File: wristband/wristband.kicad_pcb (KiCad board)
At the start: 2 copper layers, 0 parts

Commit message: Migrate wristband to NINA-B400, wire all sheets, close six design gaps
Replaces the wristband's u-blox NINA-B111 (nRF52832) with a NINA-B400-00B
(Nordic nRF52833, Bluetooth 5.1), then follows through on everything that
change and a full schematic review surfaced.

NINA-B400 migration
- New 55-pin + EGP + EAGP symbol, transcribed from the real NINA-B40 data
  sheet UBX-19049405 R09 Table 6 and cross-checked against Figure 3 for rank
  ordering. Pin numbering validated programmatically (1-55, each exactly once).
- NINA-B4 is pin/mechanically compatible with NINA-B3, NOT NINA-B1, so the
  42-pad NINA111-42 land pattern does not carry over. No official footprint
  exists anywhere -- u-blox's own Eagle library ships only NINA111-42/112-42,
  and neither KiCad's bundled nor upstream RF_Module library has a B3/B4 part.
  NINA-B400-55_PLACEHOLDER is therefore flagged: outline, pad count and rank
  arrangement are confirmed; individual pad X/Y are derived estimates.
  MUST be replaced before fabrication.
- B400 chosen over B401/B406 for its on-module U.FL connector, which let the
  PCB-side U.FL (J2) and the untuned L/C match network (L1/C13) be deleted --
  retiring the project's only open RF-tuning risk.
- No power-design impact: abs-max VCC is 3.9 V on both modules, so the MCP1700
  LDO rationale stands. Budget 12 mA -> 15.5 mA typ; ~70.5 mA with DWM3000
  against 250 mA, ~3.5x headroom (corrects a stale "3.7x" in the docs).
- SWD pin numbers are unchanged (SWDCLK=11, SWDIO=15, RESET_N=19, SWO=8).

Antenna re-verified, part number corrected
- The specified antenna is still pre-approved for NINA-B4 (certification app
  note UBX-20037320 R05 s3.2) but ProAnt was acquired by Abracon and u-blox
  now lists it as PRO-IS-237. Same specs throughout. Order under the Abracon PN.

Six gaps closed
- Y1 + C14/C15: 32.768 kHz LFXO (Epson FC-135, Q13FC13500004). Required for
  lowest sleep current per SIM UBX-19052230 R13 s1.9; XL1/XL2 were floating,
  which Table 6 does not permit eve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
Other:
- board outline added: 45 x 35 mm
- copper layers 2 -> 4
- board text added: "Wristband v0 -- 45 x 35 mm, 4-layer. Stackup intent: F.Cu signal / In1.Cu GND plane / In2.Cu power / B.Cu signal. Solid In1.Cu ground reference is required under the DWM3000 UWB and NINA-B400 BLE sections. Outline and size are a STARTING POINT -- confirm against enclosure and strap before layout."
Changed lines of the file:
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@@
 	(layers
 		(0 "F.Cu" signal)
+		(1 "In1.Cu" signal)
+		(2 "In2.Cu" signal)
 		(31 "B.Cu" signal)
 		(32 "B.Adhes" user "B.Adhesive")
@@
 	)
 	(net 0 "")
+	(gr_line
+		(start 100 60)
+		(end 145 60)
+		(stroke
+			(width 0.1)
+			(type default)
+		)
+		(layer "Edge.Cuts")
+	)
+	(gr_line
+		(start 145 60)
+		(end 145 95)
+		(stroke
+			(width 0.1)
+			(type default)
+		)
+		(layer "Edge.Cuts")
+	)
+	(gr_line
+		(start 145 95)
+		(end 100 95)
+		(stroke
+			(width 0.1)
+			(type default)
+		)
+		(layer "Edge.Cuts")
+	)
+	(gr_line
+		(start 100 95)
+		(end 100 60)
+		(stroke
+			(width 0.1)
+			(type default)
+		)
+		(layer "Edge.Cuts")
+	)
+	(gr_text "Wristband v0 -- 45 x 35 mm, 4-layer.\nStackup intent: F.Cu signal / In1.Cu GND plane / In2.Cu power / B.Cu signal.\nSolid In1.Cu ground reference is required under the DWM3000 UWB and NINA-B400 BLE sections.\nOutline and size are a STARTING POINT -- confirm against enclosure and strap before layout."
+		(at 100 101 0)
+		(layer "Cmts.User")
+		(effects
+			(font
+				(size 1.2 1.2)
+				(thickness 0.2)
+			)
+			(justify left)
+		)
+	)
 )

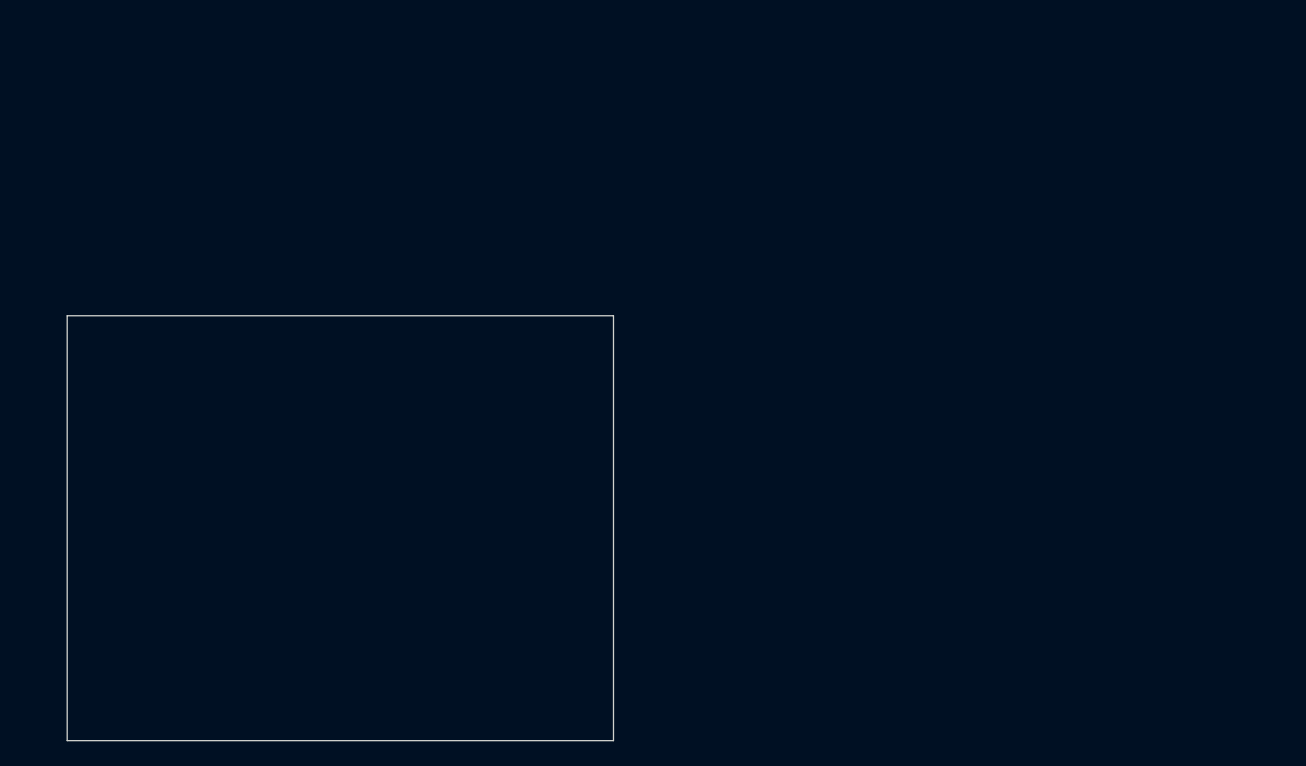
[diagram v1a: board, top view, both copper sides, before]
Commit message: Convert global labels to power symbols; import footprints to PCB
Continues the ground cleanup from 0263e7f across the rest of the wristband
sheets: global labels replaced with explicit power symbols and wired
junctions, so connections are drawn rather than implied by name.

                     wires      labels      junctions   symbols
  power_bms          61 -> 83   61 -> 51    0 -> 3      25 -> 36
  programming_debug   7 ->  8    7 ->  4    0 -> 1       1 ->  3
  radio_mcu          71 -> 79   64 -> 42    7 -> 17     18 -> 32
  regulation          7 ->  7    7 ->  4    0 -> 0       3 ->  6

The added symbols are all power ports, so the BOM is untouched: still 47
components, 76 nets, 42 no-connects, 35 analyzer findings with 1 error --
identical before and after. The one error is the known DW01A false
positive (U1.6 GND sits on CELL_N by design, per the reference circuit).

Also ran Update PCB from Schematic on the wristband: 0 -> 46 footprints.
Nothing routed yet, no zones, board outline unchanged.

Co-Authored-By: Claude Opus 5 (1M context) <noreply@anthropic.com>
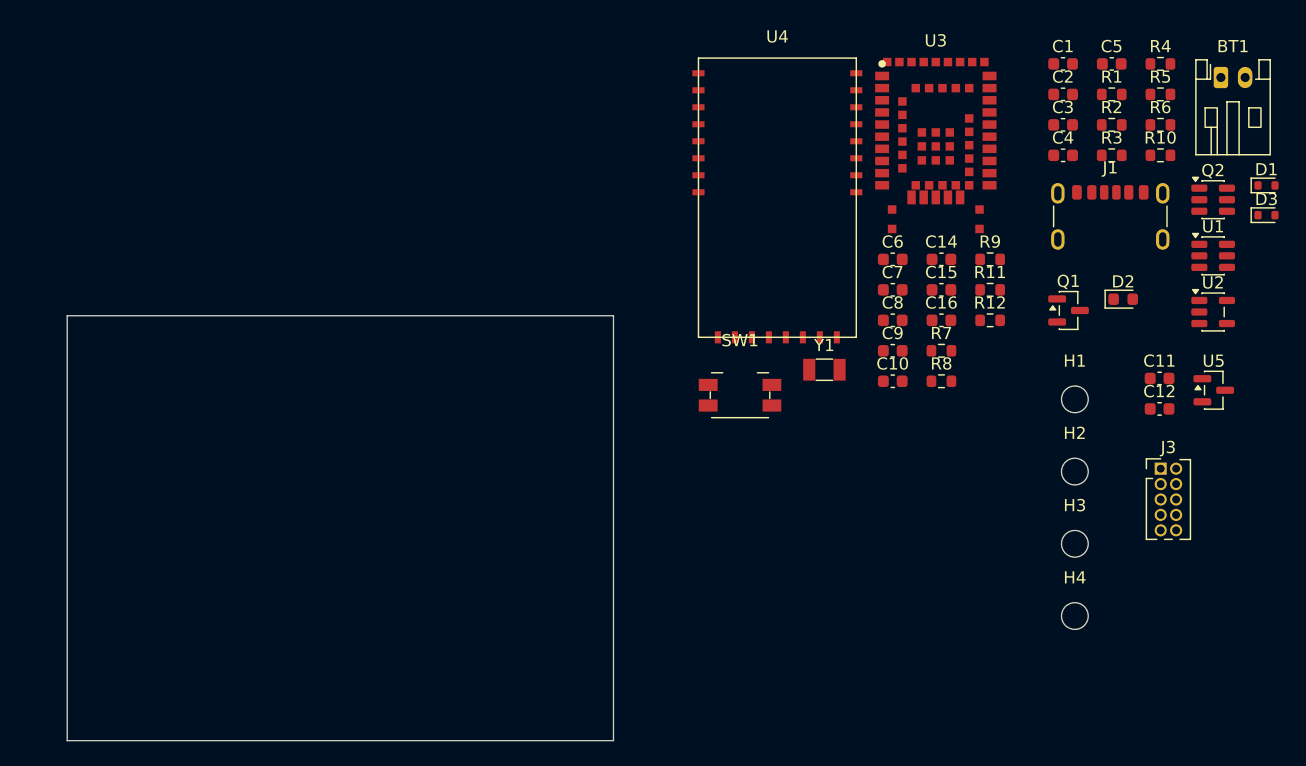
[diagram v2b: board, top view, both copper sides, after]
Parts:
- added BT1: 3.7V LiPo (1S, JST-PH 2-pin), Connector_JST:JST_PH_S2B-PH-K_1x02_P2.00mm_Horizontal, F.Cu at (195.0, 40.4)
- added C1: 0.1uF, Capacitor_SMD:C_0603_1608Metric, F.Cu at (182.0, 39.3)
- added C10: 100nF, Capacitor_SMD:C_0603_1608Metric, F.Cu at (168.0, 65.4)
- added C11: 1uF, Capacitor_SMD:C_0603_1608Metric, F.Cu at (190.0, 65.2)
- added C12: 1uF, Capacitor_SMD:C_0603_1608Metric, F.Cu at (190.0, 67.7)
- added C14: 18pF, Capacitor_SMD:C_0603_1608Metric, F.Cu at (172.0, 55.4)
- added C15: 18pF, Capacitor_SMD:C_0603_1608Metric, F.Cu at (172.0, 57.9)
- added C16: 100nF, Capacitor_SMD:C_0603_1608Metric, F.Cu at (172.0, 60.4)
- added C2: 4.7uF, Capacitor_SMD:C_0603_1608Metric, F.Cu at (182.0, 41.8)
- added C3: 4.7uF, Capacitor_SMD:C_0603_1608Metric, F.Cu at (182.0, 44.3)
- added C4: 10uF, Capacitor_SMD:C_0603_1608Metric, F.Cu at (182.0, 46.8)
- added C5: 100nF, Capacitor_SMD:C_0603_1608Metric, F.Cu at (186.0, 39.3)
- added C6: 100nF, Capacitor_SMD:C_0603_1608Metric, F.Cu at (168.0, 55.4)
- added C7: 100nF, Capacitor_SMD:C_0603_1608Metric, F.Cu at (168.0, 57.9)
- added C8: 100nF, Capacitor_SMD:C_0603_1608Metric, F.Cu at (168.0, 60.4)
- added C9: 100nF, Capacitor_SMD:C_0603_1608Metric, F.Cu at (168.0, 62.9)
- added D1: ESD5B5.0ST1G, Diode_SMD:D_SOD-523, F.Cu at (198.8, 49.3)
- added D2: Green, LED_SMD:LED_0603_1608Metric, F.Cu at (187.0, 58.6)
- added D3: ESD5B5.0ST1G, Diode_SMD:D_SOD-523, F.Cu at (198.8, 51.7)
- added H1: M2, MountingHole:MountingHole_2.2mm_M2, F.Cu at (183.0, 66.9)
- added H2: M2, MountingHole:MountingHole_2.2mm_M2, F.Cu at (183.0, 72.8)
- added H3: M2, MountingHole:MountingHole_2.2mm_M2, F.Cu at (183.0, 78.8)
- added H4: M2, MountingHole:MountingHole_2.2mm_M2, F.Cu at (183.0, 84.7)
- added J1: USB4125-GF-A, Connector_USB:USB_C_Receptacle_GCT_USB4125-xx-x_6P_TopMnt_Horizontal, F.Cu at (185.9, 52.9)
- added J3: Conn_ARM_JTAG_SWD_10, Connector_PinHeader_1.27mm:PinHeader_2x05_P1.27mm_Vertical, F.Cu at (190.1, 72.6)
- added Q1: AO3401A, Package_TO_SOT_SMD:SOT-23, F.Cu at (182.5, 59.6)
- added Q2: FS8205A, Package_TO_SOT_SMD:SOT-23-6, F.Cu at (194.4, 50.4)
- added R1: 100k, Resistor_SMD:R_0603_1608Metric, F.Cu at (186.0, 41.8)
- added R10: 1k, Resistor_SMD:R_0603_1608Metric, F.Cu at (190.1, 46.8)
- added R11: 1M, Resistor_SMD:R_0603_1608Metric, F.Cu at (176.0, 57.9)
- added R12: 1M, Resistor_SMD:R_0603_1608Metric, F.Cu at (176.0, 60.4)
- added R2: 100, Resistor_SMD:R_0603_1608Metric, F.Cu at (186.0, 44.3)
- added R3: 1k, Resistor_SMD:R_0603_1608Metric, F.Cu at (186.0, 46.8)
- added R4: 6.8k, Resistor_SMD:R_0603_1608Metric, F.Cu at (190.1, 39.3)
- added R5: 5.1k, Resistor_SMD:R_0603_1608Metric, F.Cu at (190.1, 41.8)
- added R6: 5.1k, Resistor_SMD:R_0603_1608Metric, F.Cu at (190.1, 44.3)
- added R7: 10k, Resistor_SMD:R_0603_1608Metric, F.Cu at (172.0, 62.9)
- added R8: 10k, Resistor_SMD:R_0603_1608Metric, F.Cu at (172.0, 65.4)
- added R9: 100k, Resistor_SMD:R_0603_1608Metric, F.Cu at (176.0, 55.4)
- added SW1: SOS, Button_Switch_SMD:Panasonic_EVQPUJ_EVQPUA, F.Cu at (155.4, 66.5)
- added U1: DW01A, Package_TO_SOT_SMD:SOT-23-6, F.Cu at (194.4, 55.1)
- added U2: MCP73831T-2ACI/OT, Package_TO_SOT_SMD:SOT-23-5, F.Cu at (194.4, 59.7)
- added U3: NINA-B400, wristband:NINA-B400-55_PLACEHOLDER, F.Cu at (171.6, 46.0)
- added U4: DWM3000, uwb_rescue_locator_shared:DWM3000_PLACEHOLDER, F.Cu at (158.5, 50.3)
- added U5: MCP1700T-3302E/TT, Package_TO_SOT_SMD:SOT-23, F.Cu at (194.4, 66.1)
- added Y1: 32.768kHz, Crystal:Crystal_SMD_3215-2Pin_3.2x1.5mm, F.Cu at (162.4, 64.4)

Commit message: Sync wristband PCB from schematic; board setup rules
PCB-side counterpart to the DWM3001C migration, done in the KiCad GUI
(Update PCB from Schematic), plus Board Setup changes.

- Removes the 10 footprints the migration deleted: U3, Y1, C8-C10, C14,
  C15, R7-R9. Footprint count 46 -> 36.
- U4 is now wristband:DWM3001C_PLACEHOLDER.
- Adds a physical stackup definition.
- Net classes and DRC minimums: adds FLASH_IC class, min_track_width
  0 -> 0.127mm, zone corner smoothing enabled.

INCOMPLETE - one more sync is needed. This ran before the MCP1700 ->
TPS7A0233 swap, so U5 still carries Package_TO_SOT_SMD:SOT-23 (3-pin)
while the schematic now specifies SOT-23-5, and C12 still reads 1uF
instead of 2.2uF. Re-run Update PCB from Schematic (F8).

Co-Authored-By: Claude Opus 5 (1M context) <noreply@anthropic.com>
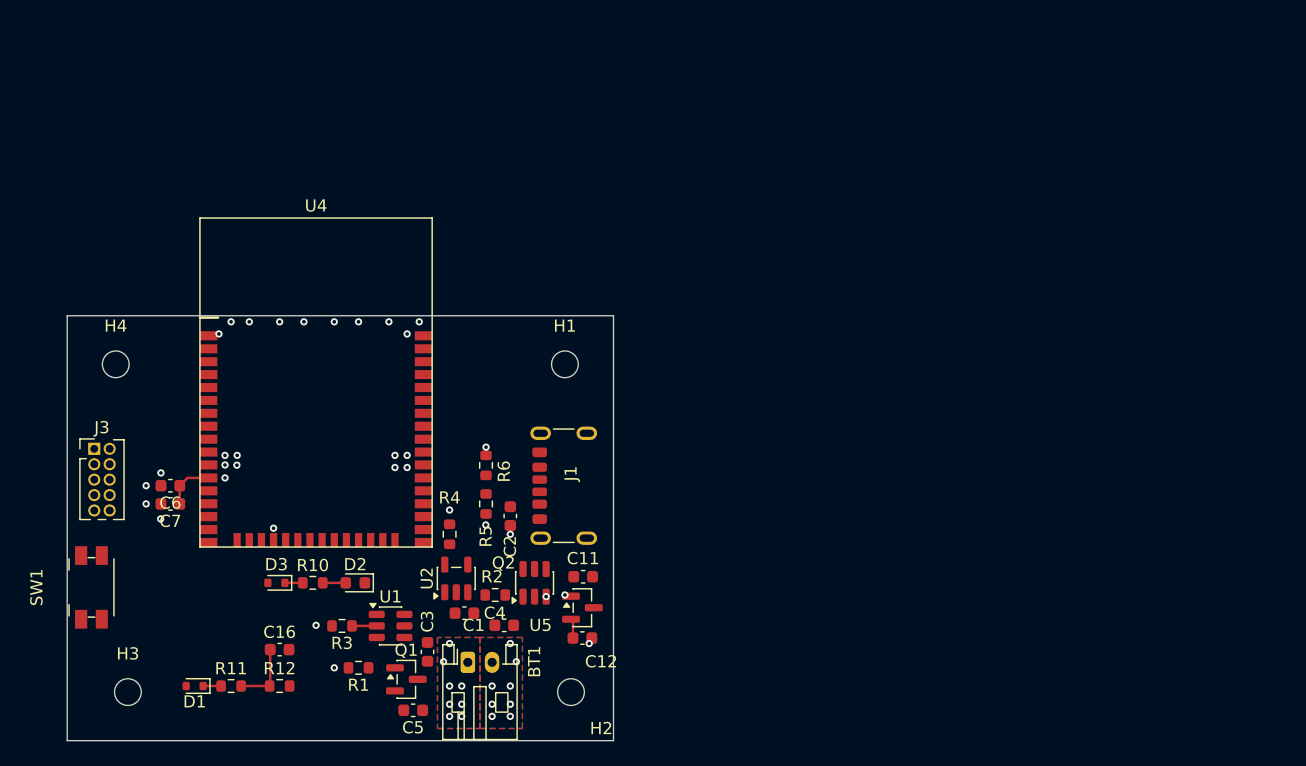
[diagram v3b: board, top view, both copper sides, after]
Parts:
- removed C10, C8, C9: 100nF, Capacitor_SMD:C_0603_1608Metric
- removed C14, C15: 18pF, Capacitor_SMD:C_0603_1608Metric
- removed R7, R8: 10k, Resistor_SMD:R_0603_1608Metric
- removed R9: 100k, Resistor_SMD:R_0603_1608Metric
- removed U3: NINA-B400, wristband:NINA-B400-55_PLACEHOLDER
- removed Y1: 32.768kHz, Crystal:Crystal_SMD_3215-2Pin_3.2x1.5mm
- C7: value 100nF -> 4.7uF
- U4: value DWM3000 -> DWM3001C; footprint uwb_rescue_locator_shared:DWM3000_PLACEHOLDER -> wristband:DWM3001C_PLACEHOLDER
- moved D1 97.4 mm to (110.5, 90.5), turned to 180 degrees
- moved J3 87.9 mm to (102.2, 71.0)
- moved D3 87.0 mm to (117.2, 82.0), turned to 180 degrees
- moved H4 81.7 mm to (104.0, 64.0)
- moved H3 79.0 mm to (105.0, 91.0)
- moved BT1 78.5 mm to (133.0, 88.5)
- moved C5 78.4 mm to (128.5, 92.5), turned to 180 degrees
- moved R10 78.2 mm to (120.2, 82.0)
- moved R1 78.0 mm to (124.0, 89.0), turned to 180 degrees
- moved R3 74.3 mm to (122.6, 85.5), turned to 180 degrees
- moved U1 74.3 mm to (126.6, 85.5)
- moved R11 70.5 mm to (113.5, 90.5)
- moved R4 70.2 mm to (131.5, 78.0), turned to 90 degrees
- moved C3 68.0 mm to (129.7, 87.7), turned to 90 degrees
- moved D2 67.4 mm to (123.7, 82.0), turned to 180 degrees
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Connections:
- net LED_A renamed Net-(D2-A)
- J1 pad SH: (no net) -> GND
- SW1 pad 1: SOS_BTN -> /Radio MCU/SOS_BNT
- U4 pad 1: unconnected-(U4-EXTON-Pad1) -> GND
- U4 pad 10: UWB_SPIPOL -> unconnected-(U4-P0.04-Pad10)
- U4 pad 11: unconnected-(U4-GPIO4-Pad11) -> GND
- U4 pad 12: unconnected-(U4-GPIO3/TXLED-Pad12) -> +3V3
- U4 pad 16: GND -> unconnected-(U4-P0.21-Pad16)
- U4 pad 17: UWB_CS -> unconnected-(U4-P0.20-Pad17)
- U4 pad 18: UWB_MOSI -> unconnected-(U4-VUSB-Pad18)
- U4 pad 19: UWB_MISO -> unconnected-(U4-USB_N-Pad19)
- U4 pad 2: UWB_WAKEUP -> SWDCLK
- U4 pad 20: UWB_CLK -> unconnected-(U4-USB_P-Pad20)
- U4 pad 22: UWB_IRQ -> unconnected-(U4-P0.11-Pad22)
- U4 pad 23: GND -> unconnected-(U4-P1.08-Pad23)
- U4 pad 24: GND -> unconnected-(U4-P0.06-Pad24)
- U4 pad 3: UWB_RSTn -> SWDIO
- U4 pad 5: +3V3 -> unconnected-(U4-P0.09/NFC1-Pad5)
- U4 pad 6: +3V3 -> /Radio MCU/SOS_BNT
- U4 pad 7: +3V3 -> unconnected-(U4-P0.14-Pad7)
- U4 pad 8: GND -> unconnected-(U4-P0.22-Pad8)
- U4 pad 9: UWB_SPIPHA -> unconnected-(U4-P0.05-Pad9)
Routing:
- net +3V3: track 0.00 -> 5.77 mm, vias 0 -> 1
- net VBAT_SENSE: track 0.00 -> 5.37 mm
- net PROT_CS: track 0.00 -> 2.04 mm
- net Net-(D2-A): track 0.00 -> 1.89 mm
- net VBAT: track 0.00 -> 1.55 mm
- net VBUS: track 0.00 -> 1.47 mm
- net GND: vias 0 -> 32
- net CELL_P: vias 0 -> 8
- net CELL_N: vias 0 -> 8
- added copper zone on B.Cu, net CELL_N
- added copper zone on F.Cu, net CELL_N
- added copper zone on In1.Cu, net CELL_N
- added copper zone on In2.Cu, net CELL_N
- added copper zone on B.Cu, net CELL_P
- added copper zone on F.Cu, net CELL_P
- added copper zone on In1.Cu, net CELL_P
- added copper zone on In2.Cu, net CELL_P
